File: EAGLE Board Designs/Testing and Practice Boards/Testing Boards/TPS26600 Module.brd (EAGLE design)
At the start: 12 x 11 mm, 10 parts

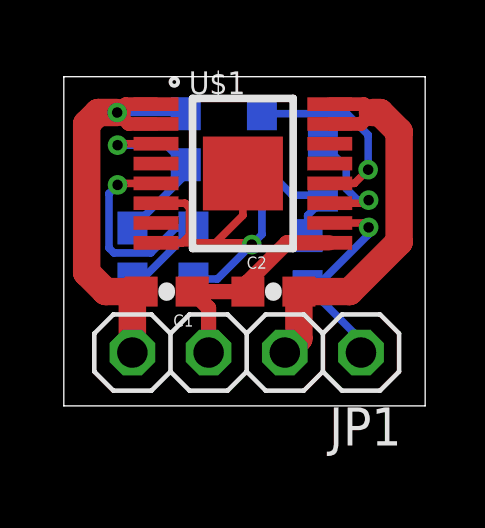
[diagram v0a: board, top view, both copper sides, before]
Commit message: Made it so that there were no drc errors
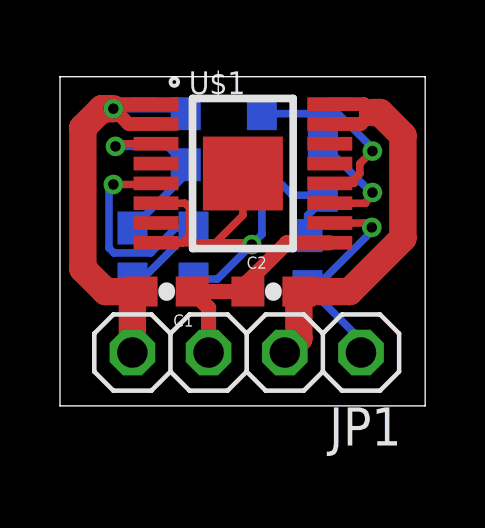
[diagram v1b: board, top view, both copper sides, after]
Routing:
- net IN: track 15.5 -> 16.0 mm
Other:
- board size 12 x 11 mm -> 12.2 x 11 mm
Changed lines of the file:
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@@
 <board>
 <plain>
-<wire x1="1.016" y1="2.921" x2="13.061" y2="2.921" width="0" layer="20"/>
+<wire x1="0.889" y1="2.921" x2="13.061" y2="2.921" width="0" layer="20"/>
 <wire x1="13.061" y1="2.921" x2="13.061" y2="13.894" width="0" layer="20"/>
-<wire x1="13.061" y1="13.894" x2="1.016" y2="13.894" width="0" layer="20"/>
-<wire x1="1.016" y1="13.894" x2="1.016" y2="2.921" width="0" layer="20"/>
+<wire x1="13.061" y1="13.894" x2="0.889" y2="13.894" width="0" layer="20"/>
+<wire x1="0.889" y1="13.894" x2="0.889" y2="2.921" width="0" layer="20"/>
 <dimension x1="1.016" y1="14.478" x2="12.954" y2="14.478" x3="6.985" y3="15.24" textsize="1.778" layer="1" dtype="vertical"/>
 <dimension x1="0" y1="2.54" x2="0" y2="13.843" x3="-2.54" y3="8.1915" textsize="1.778" layer="1" dtype="vertical"/>
@@
 <contactref element="R2" pad="2"/>
 <contactref element="U$1" pad="3"/>
-<wire x1="4.0894" y1="11.6586" x2="2.855475" y2="11.6586" width="0.254" layer="1"/>
-<wire x1="2.855475" y1="11.6586" x2="2.8086" y2="11.611725" width="0.254" layer="1"/>
-<via x="2.8086" y="11.611725" extent="1-16" drill="0.35"/>
+<via x="2.739275" y="11.5716" extent="1-16" drill="0.35"/>
 <wire x1="3.302" y1="8.851" x2="5.08" y2="10.629" width="0.254" layer="16"/>
 <wire x1="5.08" y1="10.629" x2="5.08" y2="10.961" width="0.254" layer="16"/>
-<wire x1="5.08" y1="10.961" x2="4.429275" y2="11.611725" width="0.254" layer="16"/>
-<wire x1="4.429275" y1="11.611725" x2="2.8086" y2="11.611725" width="0.254" layer="16"/>
+<wire x1="2.739275" y1="11.5716" x2="2.826275" y2="11.6586" width="0.254" layer="1"/>
+<wire x1="2.826275" y1="11.6586" x2="4.0894" y2="11.6586" width="0.254" layer="1"/>
+<wire x1="2.739275" y1="11.5716" x2="4.4694" y2="11.5716" width="0.254" layer="16"/>
+<wire x1="4.4694" y1="11.5716" x2="5.08" y2="10.961" width="0.254" layer="16"/>
 </signal>
 <signal name="N$4">
@@
 <contactref element="R3" pad="2"/>
 <contactref element="U$1" pad="5"/>
-<wire x1="4.0894" y1="10.3378" x2="2.8594" y2="10.3378" width="0.254" layer="1"/>
-<wire x1="2.8594" y1="10.3378" x2="2.8086" y2="10.287" width="0.254" layer="1"/>
-<via x="2.8086" y="10.287" extent="1-16" drill="0.35"/>
+<via x="2.667" y="10.3016" extent="1-16" drill="0.35"/>
 <wire x1="3.302" y1="7.151" x2="3.634" y2="7.151" width="0.254" layer="16"/>
 <wire x1="3.634" y1="7.151" x2="5.334" y2="8.851" width="0.254" layer="16"/>
 <wire x1="3.91773125" y1="8.0216" x2="2.68626875" y2="8.0216" width="0.254" layer="16"/>
-<wire x1="2.68626875" y1="8.0216" x2="2.5226" y2="8.18526875" width="0.254" layer="16"/>
+<wire x1="2.5226" y1="8.18526875" x2="2.68626875" y2="8.0216" width="0.254" layer="16"/>
 <wire x1="5.334" y1="8.851" x2="4.74713125" y2="8.851" width="0.254" layer="16"/>
 <wire x1="4.74713125" y1="8.851" x2="3.91773125" y2="8.0216" width="0.254" layer="16"/>
-<wire x1="2.5226" y1="10.001" x2="2.8086" y2="10.287" width="0.254" layer="16"/>
-<wire x1="2.5226" y1="8.18526875" x2="2.5226" y2="10.001" width="0.254" layer="16"/>
+<wire x1="2.667" y1="10.3016" x2="2.5226" y2="10.1572" width="0.254" layer="16"/>
+<wire x1="2.5226" y1="10.1572" x2="2.5226" y2="8.18526875" width="0.254" layer="16"/>
+<wire x1="2.667" y1="10.3016" x2="4.0532" y2="10.3016" width="0.254" layer="1"/>
+<wire x1="4.0532" y1="10.3016" x2="4.0894" y2="10.3378" width="0.254" layer="1"/>
 </signal>
 <signal name="N$6">
@@
 <wire x1="9.652" y1="11.645" x2="9.564" y2="11.645" width="0.254" layer="16"/>
 <wire x1="9.8806" y1="9.6774" x2="11.0744" y2="9.6774" width="0.254" layer="1"/>
-<wire x1="11.0744" y1="9.6774" x2="11.176" y2="9.779" width="0.254" layer="1"/>
-<via x="11.176" y="9.779" extent="1-16" drill="0.35"/>
-<wire x1="9.652" y1="11.645" x2="10.4314" y2="10.8656" width="0.254" layer="16"/>
-<wire x1="10.4314" y1="10.8656" x2="10.4314" y2="10.16" width="0.254" layer="16"/>
-<wire x1="10.4314" y1="10.16" x2="10.8124" y2="9.779" width="0.254" layer="16"/>
-<wire x1="10.8124" y1="9.779" x2="11.176" y2="9.779" width="0.254" layer="16"/>
+<wire x1="11.0744" y1="9.6774" x2="11.303" y2="10.033" width="0.254" layer="1"/>
+<via x="11.303" y="10.033" extent="1-16" drill="0.35"/>
+<wire x1="11.264" y1="10.033" x2="11.303" y2="10.033" width="0.254" layer="16"/>
+<wire x1="9.652" y1="11.645" x2="11.264" y2="10.033" width="0.254" layer="16"/>
 </signal>
 <signal name="N$8">
@@
 <contactref element="C3" pad="2"/>
 <wire x1="7.581" y1="12.661" x2="7.62" y2="12.661" width="0.254" layer="16"/>
-<wire x1="9.8806" y1="10.3378" x2="10.7033" y2="10.3378" width="0.254" layer="1"/>
-<wire x1="10.7033" y1="10.3378" x2="11.1605" y2="10.795" width="0.254" layer="1"/>
-<via x="11.1605" y="10.795" extent="1-16" drill="0.35"/>
-<wire x1="7.62" y1="12.661" x2="10.453" y2="12.661" width="0.254" layer="16"/>
-<wire x1="11.1605" y1="11.9535" x2="11.1605" y2="10.795" width="0.254" layer="16"/>
-<wire x1="10.453" y1="12.661" x2="11.1605" y2="11.9535" width="0.254" layer="16"/>
+<wire x1="9.8806" y1="10.3378" x2="10.16" y2="10.3378" width="0.254" layer="1"/>
+<via x="11.303" y="11.4145" extent="1-16" drill="0.35"/>
+<wire x1="10.5573125" y1="10.3378" x2="10.7033" y2="10.3378" width="0.254" layer="1"/>
+<wire x1="7.62" y1="12.661" x2="10.16" y2="12.661" width="0.254" layer="16"/>
+<wire x1="10.16" y1="12.661" x2="11.303" y2="11.518" width="0.254" layer="16"/>
+<wire x1="11.303" y1="11.518" x2="11.303" y2="11.4145" width="0.254" layer="16"/>
+<wire x1="10.8839" y1="10.6643875" x2="10.8839" y2="10.9954" width="0.254" layer="1"/>
+<wire x1="10.8839" y1="10.9954" x2="11.303" y2="11.4145" width="0.254" layer="1"/>
+<wire x1="10.16" y1="10.3378" x2="10.5573125" y2="10.3378" width="0.254" layer="1"/>
+<wire x1="10.5573125" y1="10.3378" x2="10.8839" y2="10.6643875" width="0.254" layer="1"/>
 </signal>
 <signal name="IN">
@@
 <contactref element="C1" pad="2"/>
 <contactref element="R1" pad="2"/>
-<wire x1="4.0894" y1="12.319" x2="3.175" y2="12.319" width="0.4572" layer="1"/>
-<wire x1="2.794" y1="12.7" x2="3.175" y2="12.319" width="0.4572" layer="1"/>
-<wire x1="3.0734" y1="12.9794" x2="2.794" y2="12.7" width="0.4572" layer="1"/>
-<wire x1="3.0734" y1="12.9794" x2="4.0894" y2="12.9794" width="0.4572" layer="1"/>
-<via x="2.794" y="12.7" extent="1-16" drill="0.35"/>
+<via x="2.667" y="12.827" extent="1-16" drill="0.35"/>
 <wire x1="5.08" y1="12.661" x2="5.041" y2="12.7" width="0.254" layer="16"/>
-<wire x1="5.041" y1="12.7" x2="2.794" y2="12.7" width="0.254" layer="16"/>
-<wire x1="2.794" y1="12.7" x2="2.159" y2="12.7" width="0.9144" layer="1"/>
-<wire x1="2.159" y1="12.7" x2="1.778" y2="12.319" width="0.9144" layer="1"/>
-<wire x1="1.778" y1="12.319" x2="1.778" y2="7.366" width="0.9144" layer="1"/>
+<wire x1="1.651" y1="7.493" x2="1.651" y2="12.192" width="0.9144" layer="1"/>
 <wire x1="2.413" y1="6.731" x2="3.595" y2="6.731" width="0.9144" layer="1"/>
-<wire x1="1.778" y1="7.366" x2="2.413" y2="6.731" width="0.9144" layer="1"/>
+<wire x1="1.651" y1="7.493" x2="2.413" y2="6.731" width="0.9144" layer="1"/>
 <wire x1="3.595" y1="6.731" x2="3.302" y2="6.438" width="0.9144" layer="1"/>
 <wire x1="3.302" y1="6.438" x2="3.302" y2="4.699" width="0.9144" layer="1"/>
+<wire x1="4.0894" y1="12.319" x2="3.175" y2="12.319" width="0.4572" layer="1"/>
+<wire x1="3.175" y1="12.319" x2="2.667" y2="12.827" width="0.4572" layer="1"/>
+<wire x1="4.0894" y1="12.9794" x2="2.8194" y2="12.9794" width="0.4572" layer="1"/>
+<wire x1="2.8194" y1="12.9794" x2="2.667" y2="12.827" width="0.4572" layer="1"/>
+<wire x1="1.651" y1="12.192" x2="2.286" y2="12.827" width="0.9144" layer="1"/>
+<wire x1="2.286" y1="12.827" x2="2.667" y2="12.827" width="0.9144" layer="1"/>
+<wire x1="2.667" y1="12.827" x2="4.914" y2="12.827" width="0.254" layer="16"/>
+<wire x1="4.914" y1="12.827" x2="5.08" y2="12.661" width="0.254" layer="16"/>
 </signal>
 <signal name="IMON">
@@
 <contactref element="JP1" pad="1"/>
 <wire x1="9.144" y1="6.897" x2="8.802" y2="7.239" width="0.254" layer="16"/>
-<wire x1="9.8806" y1="9.017" x2="11.0292" y2="9.017" width="0.254" layer="1"/>
-<wire x1="11.0292" y1="9.017" x2="11.176" y2="8.8702" width="0.254" layer="1"/>
-<via x="11.176" y="8.8702" extent="1-16" drill="0.35"/>
+<wire x1="11.0292" y1="9.017" x2="9.8806" y2="9.017" width="0.254" layer="1"/>
 <wire x1="9.144" y1="6.897" x2="9.2905" y2="6.7505" width="0.254" layer="16"/>
 <wire x1="9.2905" y1="6.7505" x2="10.922" y2="5.119" width="0.254" layer="16"/>
 <wire x1="10.922" y1="5.119" x2="10.922" y2="4.699" width="0.254" layer="16"/>
-<wire x1="11.176" y1="8.8702" x2="11.176" y2="8.636" width="0.254" layer="16"/>
-<wire x1="11.176" y1="8.636" x2="9.2905" y2="6.7505" width="0.254" layer="16"/>
+<wire x1="11.2832375" y1="8.7432375" x2="11.2832375" y2="8.8702" width="0.254" layer="16"/>
+<via x="11.2832375" y="8.8702" extent="1-16" drill="0.35"/>
+<wire x1="11.2832375" y1="8.8702" x2="11.176" y2="8.8702" width="0.254" layer="1"/>
+<wire x1="11.176" y1="8.8702" x2="11.0292" y2="9.017" width="0.254" layer="1"/>
+<wire x1="9.2905" y1="6.7505" x2="11.2832375" y2="8.7432375" width="0.254" layer="16"/>
 </signal>
 <signal name="OUT">
@@
 <contactref element="JP1" pad="2"/>
 <wire x1="11.303" y1="12.7" x2="11.557" y2="12.7" width="0.9144" layer="1"/>
-<wire x1="11.557" y1="12.7" x2="12.192" y2="12.065" width="0.9144" layer="1"/>
-<wire x1="12.192" y1="12.065" x2="12.192" y2="8.382" width="0.9144" layer="1"/>
+<wire x1="11.557" y1="12.7" x2="12.319" y2="11.938" width="0.9144" layer="1"/>
+<wire x1="12.319" y1="11.938" x2="12.319" y2="8.509" width="0.9144" layer="1"/>
 <wire x1="10.541" y1="6.731" x2="8.851" y2="6.731" width="0.9144" layer="1"/>
-<wire x1="12.192" y1="8.382" x2="10.541" y2="6.731" width="0.9144" layer="1"/>
+<wire x1="12.319" y1="8.509" x2="10.541" y2="6.731" width="0.9144" layer="1"/>
 <wire x1="8.851" y1="6.731" x2="8.851" y2="5.168" width="0.9144" layer="1"/>
 <wire x1="8.851" y1="5.168" x2="8.382" y2="4.699" width="0.9144" layer="1"/>
